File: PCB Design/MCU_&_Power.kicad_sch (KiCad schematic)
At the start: 0 parts

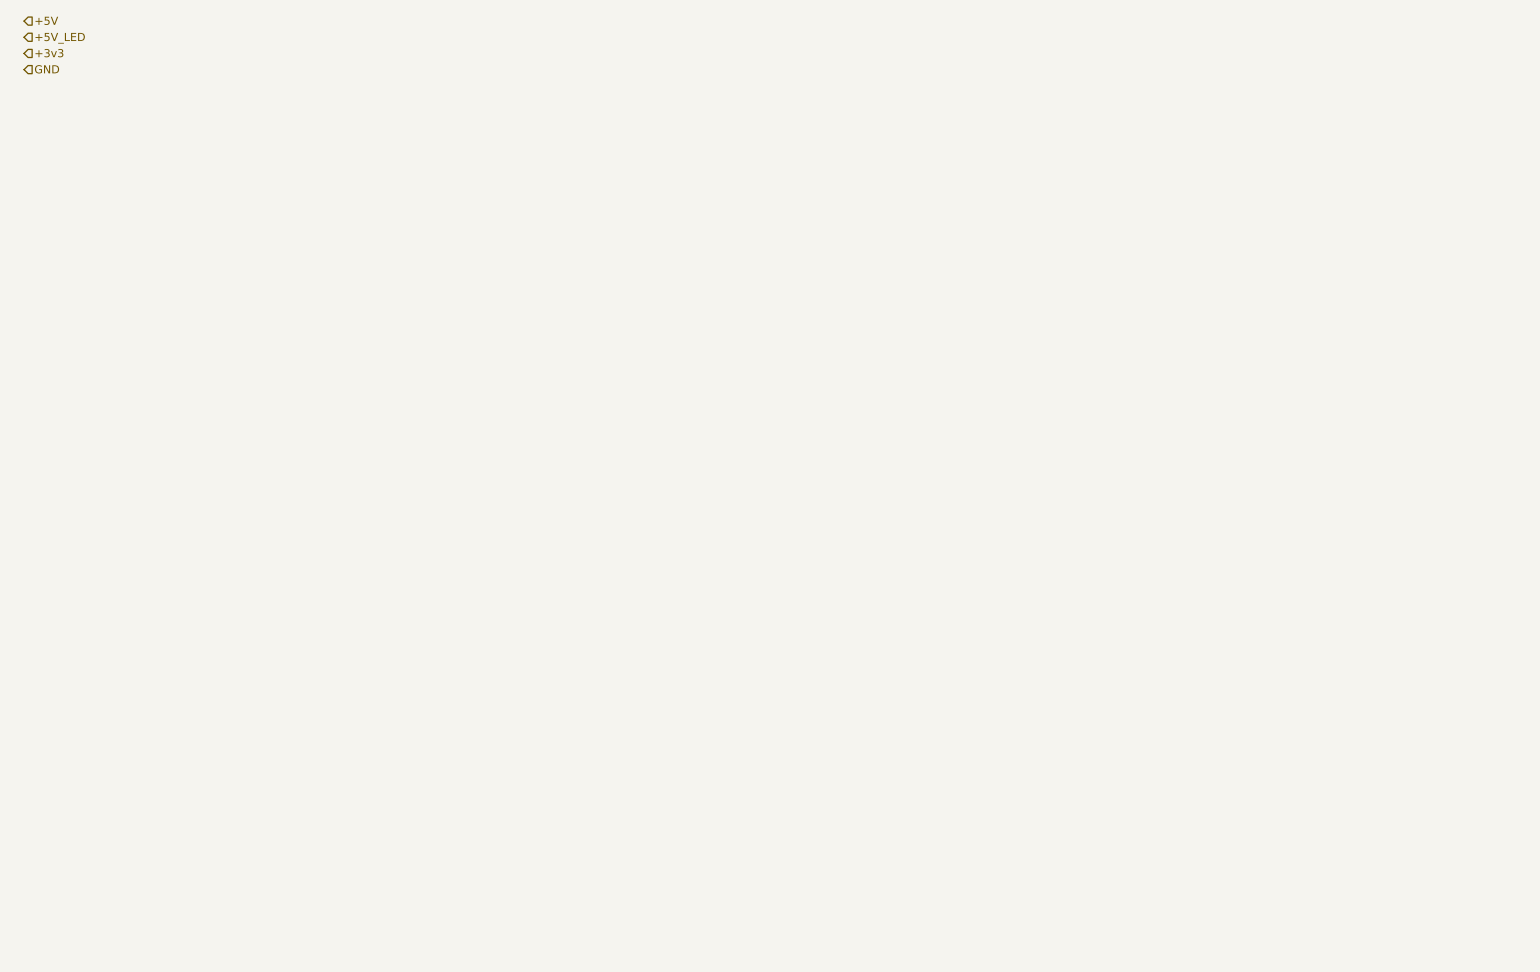
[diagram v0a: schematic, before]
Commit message: Add encoders and switches to schematic
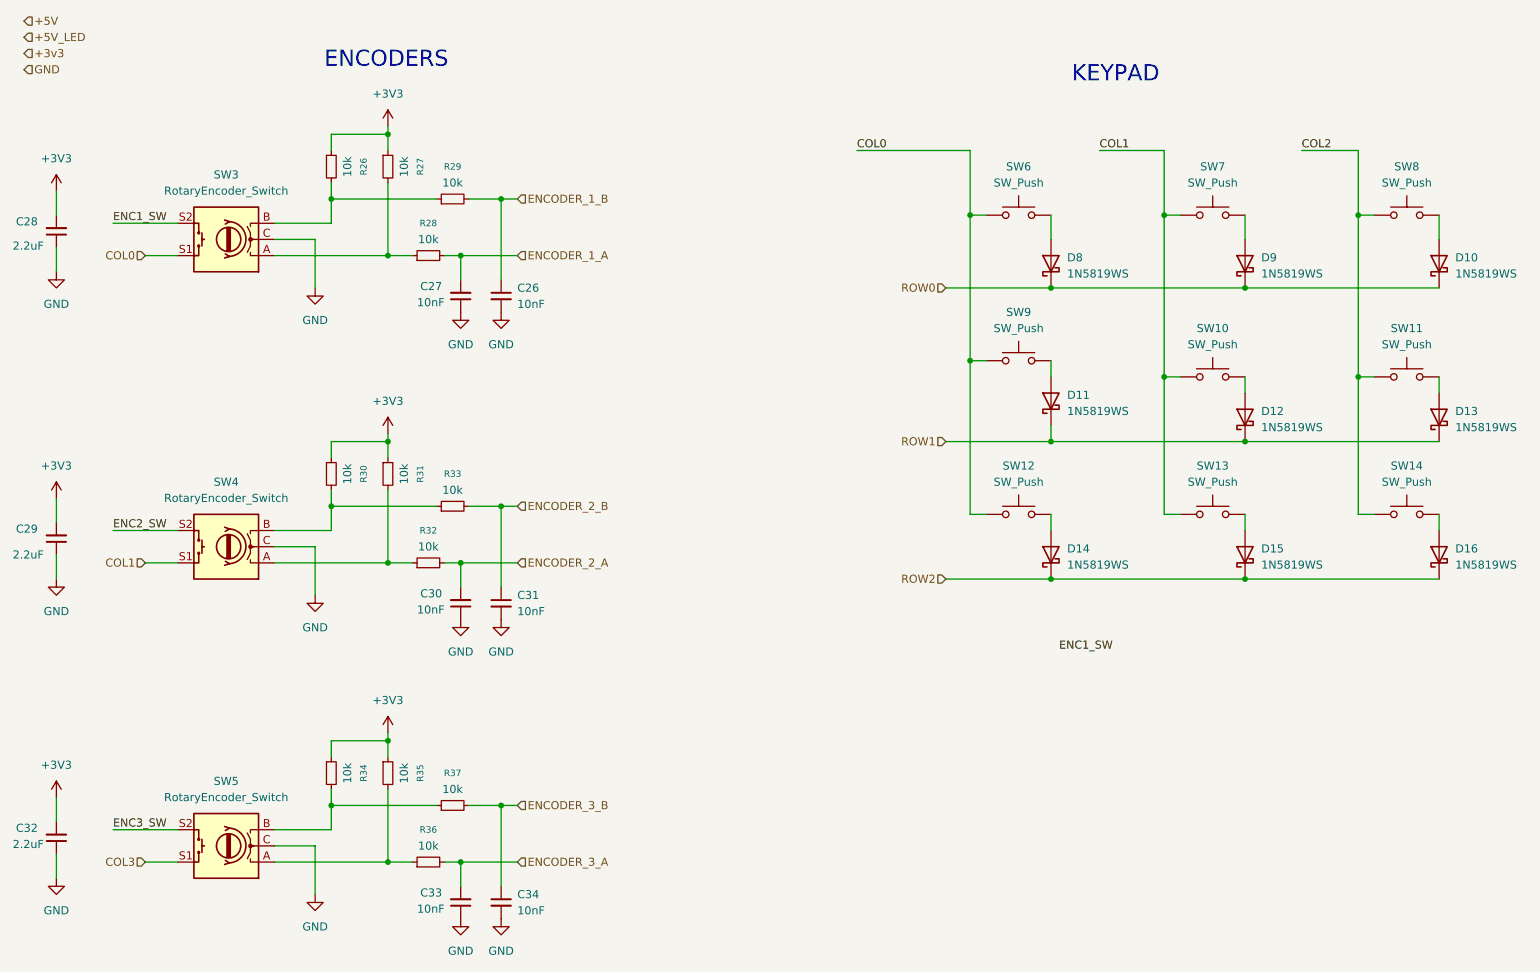
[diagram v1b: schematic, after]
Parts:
- added C26, C27, C30, C31, C33, C34: 10nF, symbol Device:C_Small
- added C28, C29, C32: 2.2uF, symbol Device:C_Small
- added D10, D11, D12, D13, D14, D15, D16, D8, D9: 1N5819WS, Diode_SMD:D_SOD-323, symbol Diode:1N5819WS
- added R26, R27, R28, R29, R30, R31, R32, R33, R34, R35, R36, R37: 10k, symbol Device:R_Small
- added SW10, SW11, SW12, SW13, SW14, SW6, SW7, SW8, SW9: SW_Push, symbol Switch:SW_Push
- added SW3, SW4, SW5: RotaryEncoder_Switch, symbol Device:RotaryEncoder_Switch
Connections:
- net GND: now also C26.2, C27.1, C28.1, C29.1, C30.1, C31.2, C32.1, C33.1, C34.2, SW3.C, SW4.C, SW5.C
- new net: D16.2 (A), SW14.2
- new net: R27.2, R28.1, SW3.A
- new net: R26.2, R29.1, SW3.B
- new net: D9.2 (A), SW7.2
- new net: R30.2, R33.1, SW4.B
- new net: D10.2 (A), SW8.2
- new net: R34.2, R37.1, SW5.B
- new net: D8.2 (A), SW6.2
- new net: D12.2 (A), SW10.2
- new net: R31.2, R32.1, SW4.A
- new net: D13.2 (A), SW11.2
- new net: D14.2 (A), SW12.2
- new net: R35.2, R36.1, SW5.A
- new net: D11.2 (A), SW9.2
- new net: D15.2 (A), SW13.2
- new net +3V3: C28.2, C29.2, C32.2, R26.1, R27.1, R30.1, R31.1, R34.1, R35.1
- new net COL0: SW12.1, SW3.S1, SW6.1, SW9.1
- new net COL1: SW10.1, SW13.1, SW4.S1, SW7.1
- new net COL2: SW11.1, SW14.1, SW8.1
- new net COL3: SW5.S1
- new net ENC1_SW: SW3.S2
- new net ENC2_SW: SW4.S2
- new net ENC3_SW: SW5.S2
- new net ENCODER_1_A: C27.2, R28.2
- new net ENCODER_1_B: C26.1, R29.2
- new net ENCODER_2_A: C30.2, R32.2
- new net ENCODER_2_B: C31.1, R33.2
- new net ENCODER_3_A: C33.2, R36.2
- new net ENCODER_3_B: C34.1, R37.2
- new net ROW0: D10.1 (K), D8.1 (K), D9.1 (K)
- new net ROW1: D11.1 (K), D12.1 (K), D13.1 (K)
- new net ROW2: D14.1 (K), D15.1 (K), D16.1 (K)
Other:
- note added: "ENCODERS"
- note added: "KEYPAD"

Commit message: Finish keys & encoder on schematic
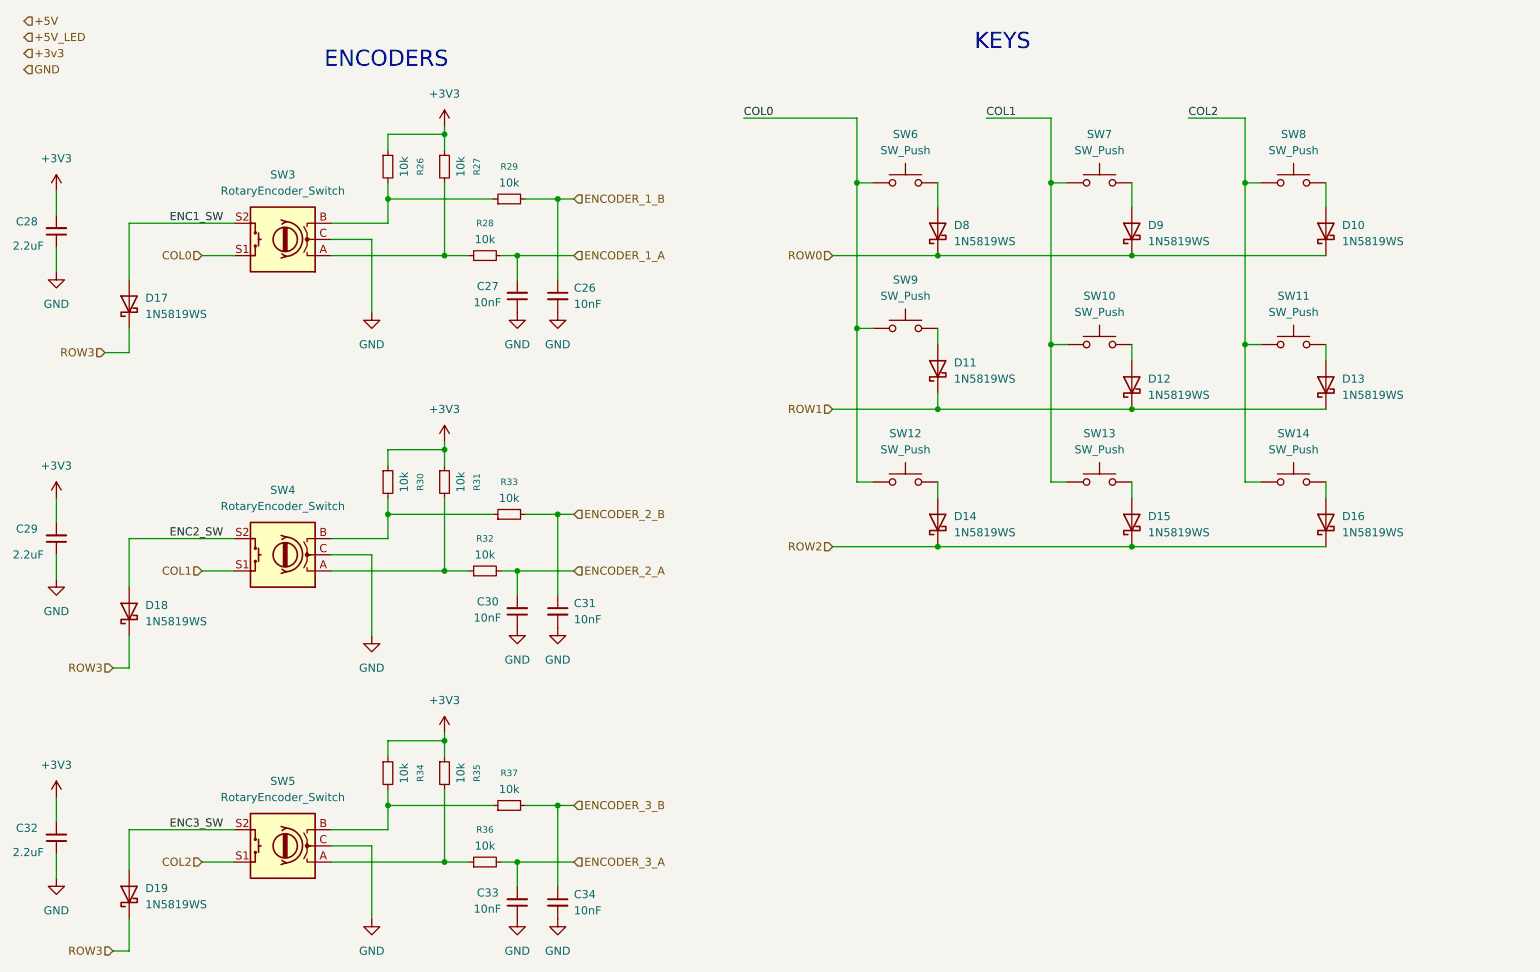
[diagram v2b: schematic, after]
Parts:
- added D17, D18, D19: 1N5819WS, Diode_SMD:D_SOD-323, symbol Diode:1N5819WS
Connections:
- net COL3 is gone; now on net COL2: SW5.S1
- net ENC1_SW: now also D17.2 (A)
- net ENC2_SW: now also D18.2 (A)
- net ENC3_SW: now also D19.2 (A)
- new net ROW3: D17.1 (K), D18.1 (K), D19.1 (K)
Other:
- note added: "KEYS"
- note removed: "KEYPAD"
- moved on the sheet: C26, C27, C30, C31, C33, C34, D10, D11, D12, D13, D14, D15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

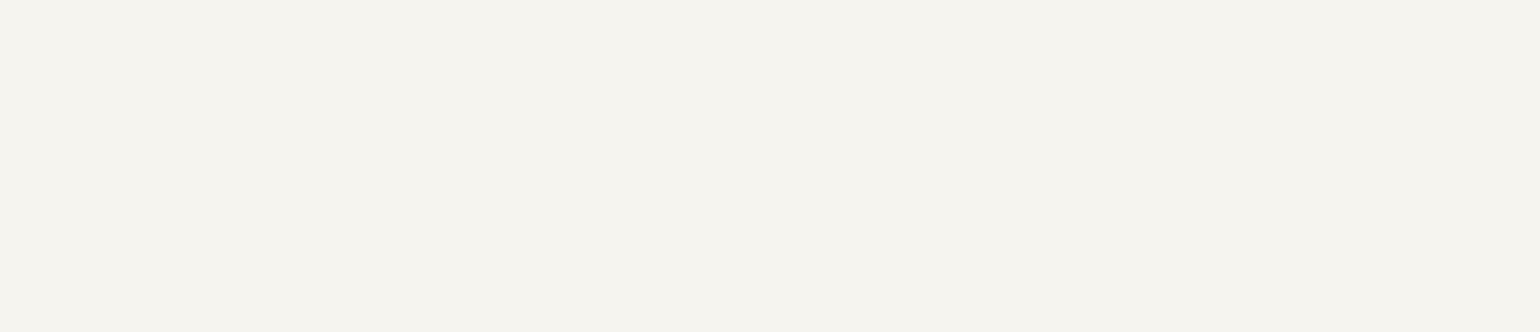
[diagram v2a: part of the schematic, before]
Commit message: Add underkey LEDs to schematic
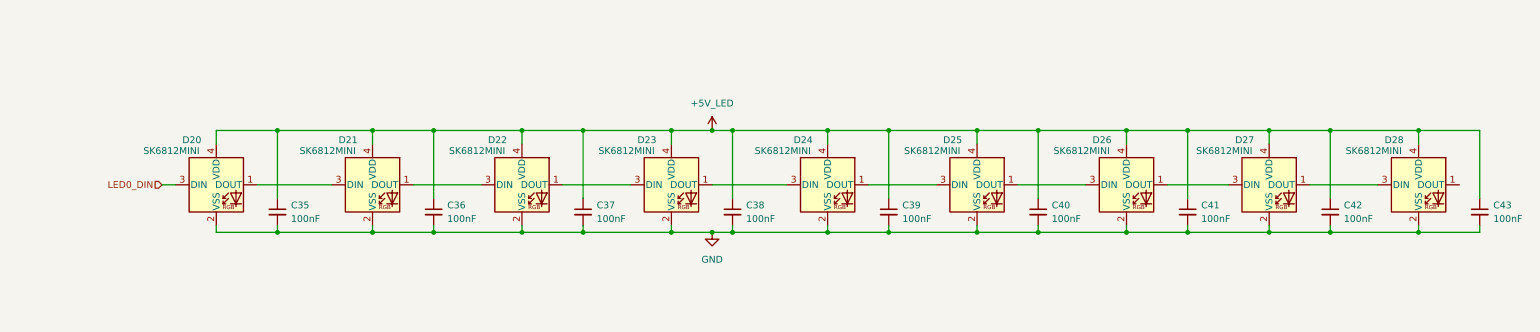
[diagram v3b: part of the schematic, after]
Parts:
- added C35, C36, C37, C38, C39, C40, C41, C42, C43: 100nF, symbol Device:C_Small
- added D20, D21, D22, D23, D24, D25, D26, D27, D28: SK6812MINI, LED_SMD:LED_SK6812MINI_PLCC4_3.5x3.5mm_P1.75mm, symbol LED:SK6812MINI
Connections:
- net +5V_LED: now also C35.1, C36.1, C37.1, C38.1, C39.1, C40.1, C41.1, C42.1, C43.1, D20.4 (VDD), D21.4 (VDD), D22.4 (VDD), D23.4 (VDD), D24.4 (VDD), D25.4 (VDD), D26.4 (VDD), D27.4 (VDD), D28.4 (VDD)
- net GND: now also C35.2, C36.2, C37.2, C38.2, C39.2, C40.2, C41.2, C42.2, C43.2, D20.2 (VSS), D21.2 (VSS), D22.2 (VSS), D23.2 (VSS), D24.2 (VSS), D25.2 (VSS), D26.2 (VSS), D27.2 (VSS), D28.2 (VSS)
- new net: D22.1 (DOUT), D23.3 (DIN)
- new net: D21.1 (DOUT), D22.3 (DIN)
- new net: D27.1 (DOUT), D28.3 (DIN)
- new net: D26.1 (DOUT), D27.3 (DIN)
- new net: D25.1 (DOUT), D26.3 (DIN)
- new net: D24.1 (DOUT), D25.3 (DIN)
- new net: D20.1 (DOUT), D21.3 (DIN)
- new net: D23.1 (DOUT), D24.3 (DIN)
- new net LED0_DIN: D20.3 (DIN)

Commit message: Add mounting holes, fix some ERC errors
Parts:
- added H1: MountingHole_Pad_MP, symbol Mechanical:MountingHole_Pad_MP
- added H2, H3, H4: MountingHole_Pad, symbol Mechanical:MountingHole_Pad
- added H5, H6, H7, H8: STANDOFF_M2.5x3.5MM, symbol Mechanical:MountingHole_Pad
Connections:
- net GND: now also H1.MP, H2.1, H3.1, H4.1, H5.1, H6.1, H7.1, H8.1
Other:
- note added: "KEYSWITCH LED LIGHTING"
- moved on the sheet: C26, C27, C28, C29, C30, C31, C32, C33, C34, C35, C36, C37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

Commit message: More ERC fixes
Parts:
- added C25: 1uF, symbol Device:C_Small
- added R25: 100M, symbol Device:R_Small
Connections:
- net GND: now also C25.1
- net +5V_LED: no longer names the net of C35.1, C36.1, C37.1, C38.1, C39.1, C40.1, C41.1, C42.1, C43.1, D20.4 (VDD), D21.4 (VDD), D22.4 (VDD), D23.4 (VDD), D24.4 (VDD), D25.4 (VDD), D26.4 (VDD), D27.4 (VDD), D28.4 (VDD)
- net +5V_LED: now also C25.2, R25.1
- new net +5V: R25.2
- no-connect marks 0 -> 1
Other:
- moved on the sheet: C35, C36, C37, C38, C39, C40, C41, C42, C43, D20, D21, D22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
